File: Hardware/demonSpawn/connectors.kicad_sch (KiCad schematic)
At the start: 22 parts, among them J1 TYPE-C-31-M-12, J2 LED1_CONN, J3 LED2_CONN, SW1 SKRPARE010, SW2 SKRPARE010, SW3 SKRPARE010, SW4 SKRPARE010, SW5 ON_OFF_BTN, U1 USBLC6-2SC6

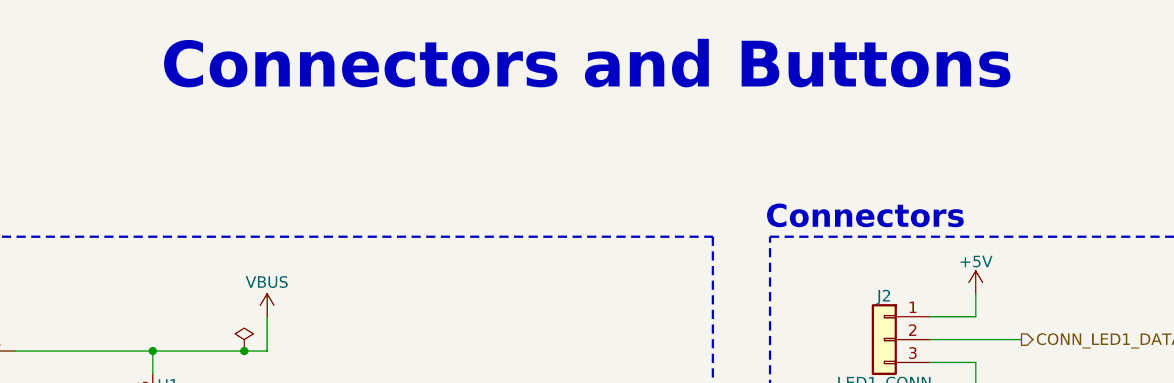
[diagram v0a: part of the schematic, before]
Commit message: doc: Add schematic pdf
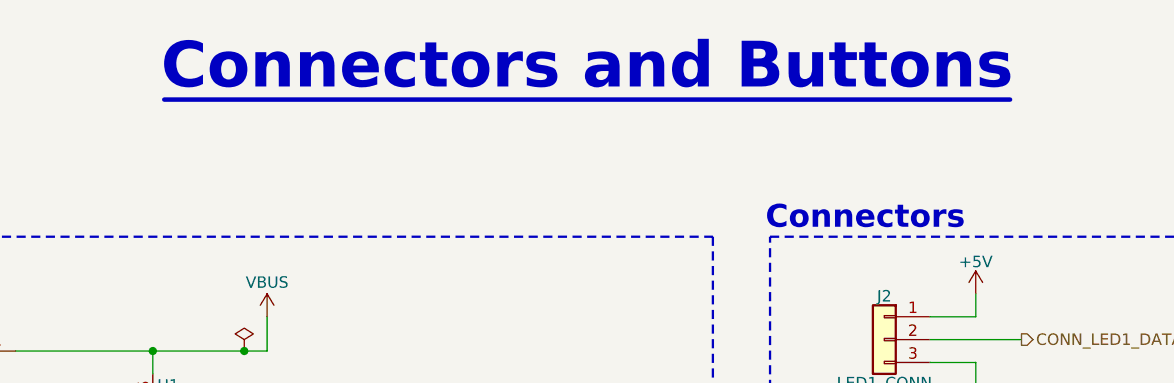
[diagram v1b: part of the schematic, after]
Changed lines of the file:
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@@
+		)
+	)
+	(polyline
+		(pts
+			(xy 104.14 21.59) (xy 198.12 21.59)
+		)
+		(stroke
+			(width 0.5)
+			(type solid)
 		)
 	)
